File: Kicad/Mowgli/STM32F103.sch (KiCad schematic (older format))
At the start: 1 part

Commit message: added LIS example code
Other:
- note added: "(I2C Accelerometer)"
- note added: "(SPI3 Flash)"
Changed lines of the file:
@@
 encoding utf-8
 Sheet 3 9
-Title ""
-Date ""
-Rev ""
+Title "Project Mowgli"
+Date "2022-05-22"
+Rev "1.0.1"
 Comp ""
-Comment1 ""
-Comment2 ""
+Comment1 "(c) CyberNet / cn@warp.at"
+Comment2 "https://github.com/cloudn1ne/Mowgli"
 Comment3 ""
 Comment4 ""
@@
 Wire Wire Line
 	7200 3800 6450 3800
+Text Notes 7700 3800 0    50   ~ 0
+(I2C Accelerometer)
+Text Notes 7650 3550 0    50   ~ 0
+(SPI3 Flash)
 $EndSCHEMATC

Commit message: updated Kicad with Charge/Battery Circuit
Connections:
- net CHARGE_LOW_SIDE_DRIVER: now reaches U?.39 (PE8)
- net CHARGE_HIGHSIDE_DRIVER: now reaches U?.40 (PE9)
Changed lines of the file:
@@
 $Descr A4 11693 8268
 encoding utf-8
-Sheet 3 9
+Sheet 3 10
 Title "Project Mowgli"
 Date "2022-05-22"
@@
 Text Notes 7650 3550 0    50   ~ 0
 (SPI3 Flash)
+Text HLabel 3700 3900 0    50   Output ~ 0
+CHARGE_LOW_SIDE_DRIVER
+Text HLabel 3700 4000 0    50   Output ~ 0
+CHARGE_HIGHSIDE_DRIVER
+Wire Wire Line
+	4450 3900 3700 3900
+Wire Wire Line
+	4450 4000 3700 4000
 $EndSCHEMATC

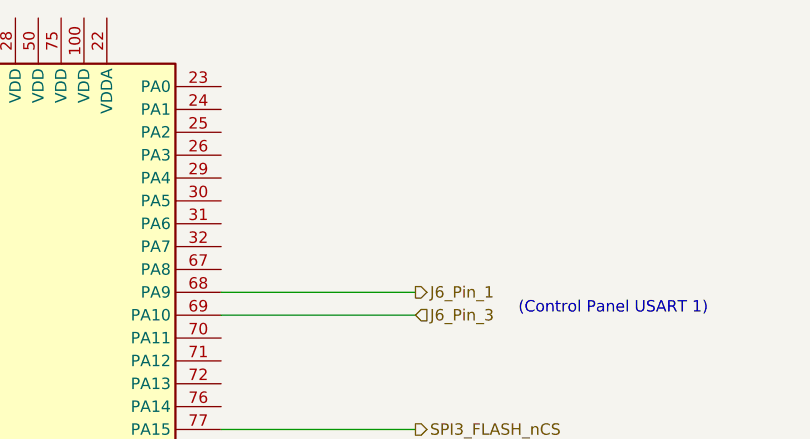
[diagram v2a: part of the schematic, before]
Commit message: added PA3 ADC input pin
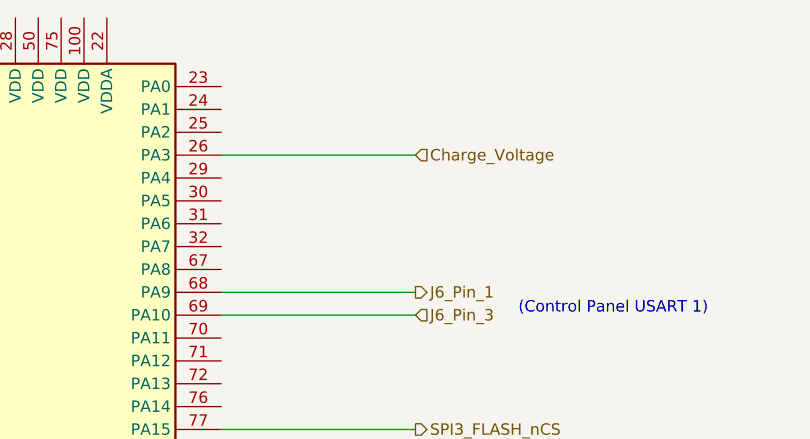
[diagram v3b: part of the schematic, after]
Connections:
- net Charge_Voltage: now reaches U?.26 (PA3)
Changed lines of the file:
@@
 Wire Wire Line
 	4450 4000 3700 4000
+Text HLabel 7300 1700 2    50   Input ~ 0
+Charge_Voltage
+Wire Wire Line
+	7300 1700 6450 1700
 $EndSCHEMATC

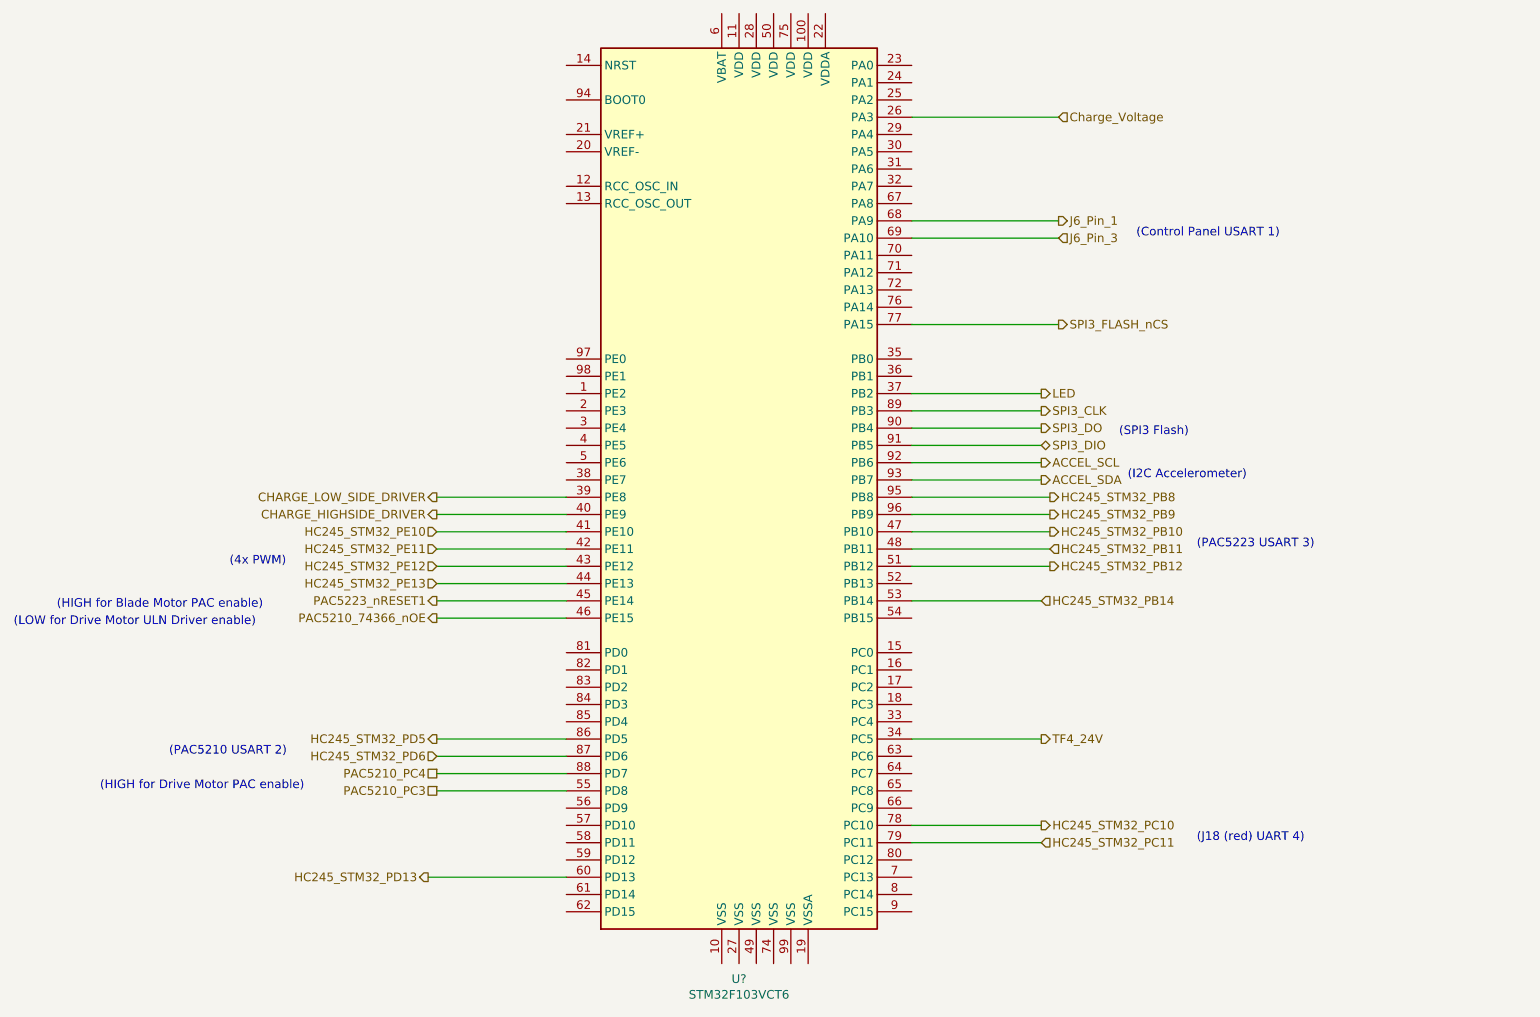
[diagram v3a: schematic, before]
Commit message: added in/out ports that could be found in ghidra
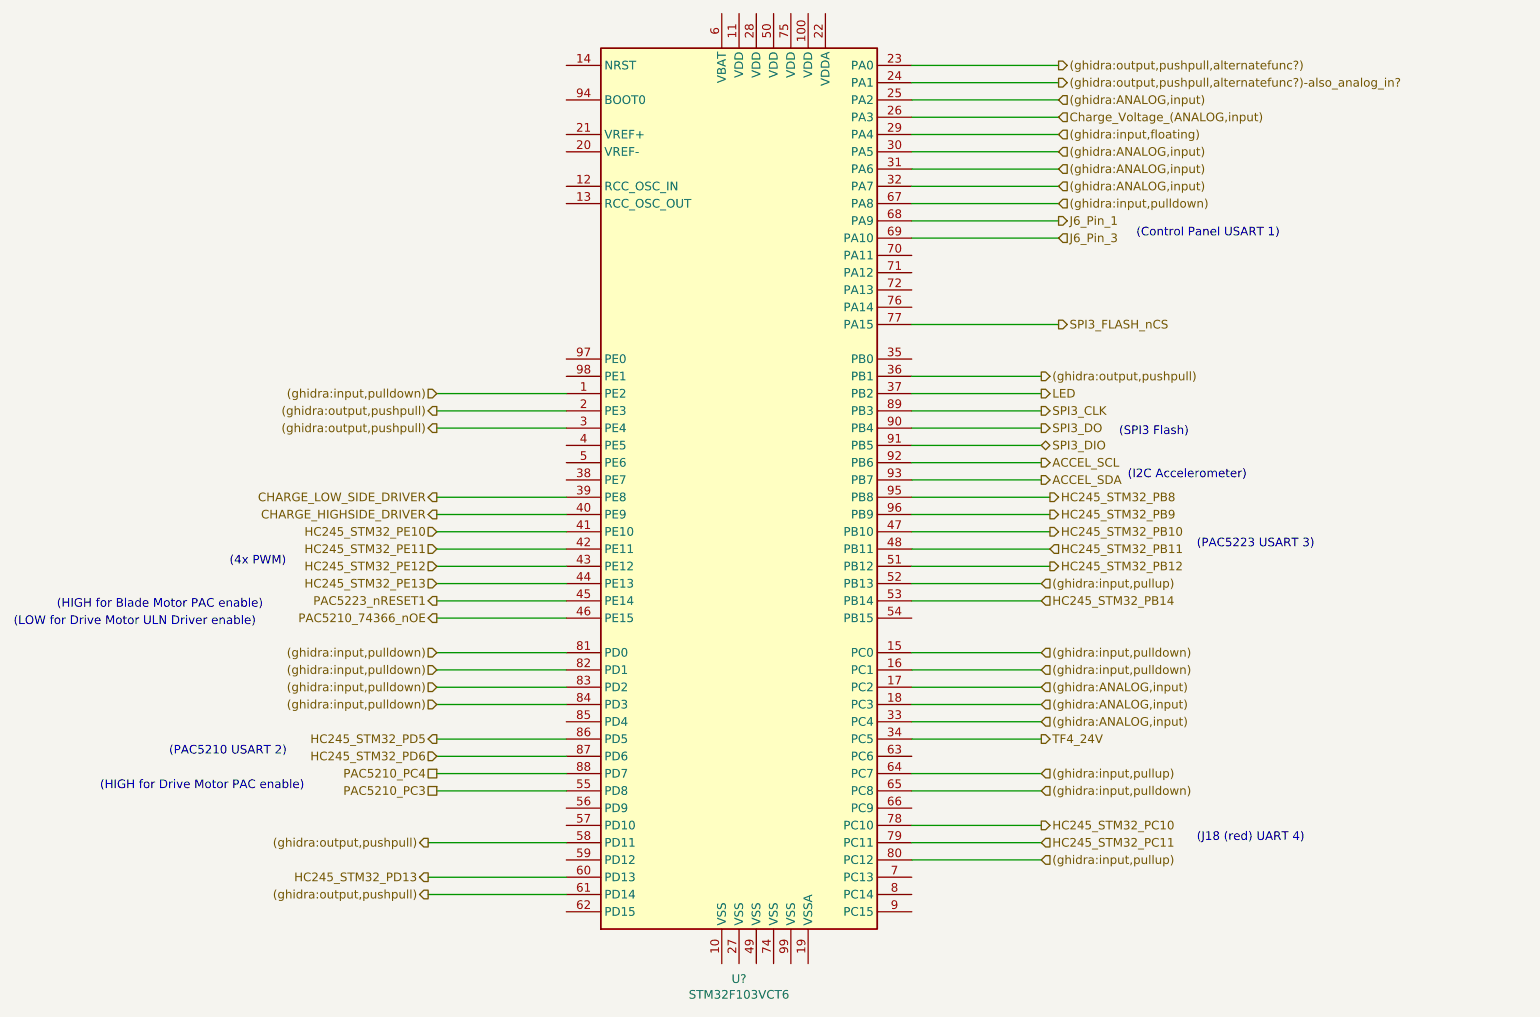
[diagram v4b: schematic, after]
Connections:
- net (ghidra:input,pulldown): now reaches U?.1 (PE2)
- net (ghidra:input,pulldown): now also U?.15 (PC0), U?.16 (PC1), U?.65 (PC8), U?.67 (PA8), U?.81 (PD0), U?.82 (PD1), U?.83 (PD2), U?.84 (PD3)
- net (ghidra:ANALOG,input): now reaches U?.17 (PC2)
- net (ghidra:ANALOG,input): now also U?.18 (PC3), U?.25 (PA2), U?.30 (PA5), U?.31 (PA6), U?.32 (PA7), U?.33 (PC4)
- net (ghidra:output,pushpull): now reaches U?.2 (PE3)
- net (ghidra:output,pushpull): now also U?.3 (PE4), U?.36 (PB1), U?.58 (PD11), U?.61 (PD14)
- net (ghidra:output,pushpull,alternatefunc?): now reaches U?.23 (PA0)
- net (ghidra:output,pushpull,alternatefunc?)-also_analog_in?: now reaches U?.24 (PA1)
- net (ghidra:input,floating): now reaches U?.29 (PA4)
- net (ghidra:input,pullup): now reaches U?.52 (PB13)
- net (ghidra:input,pullup): now also U?.64 (PC7), U?.80 (PC12)
- net Charge_Voltage renamed Charge_Voltage_(ANALOG,input)
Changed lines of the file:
@@
 	4450 4000 3700 4000
 Text HLabel 7300 1700 2    50   Input ~ 0
-Charge_Voltage
+Charge_Voltage_(ANALOG,input)
 Wire Wire Line
 	7300 1700 6450 1700
+Text HLabel 7300 2200 2    50   Input ~ 0
+(ghidra:input,pulldown)
+Wire Wire Line
+	7300 2200 6450 2200
+Text HLabel 3700 5000 0    50   Input ~ 0
+(ghidra:input,pulldown)
+Text HLabel 3700 5100 0    50   Input ~ 0
+(ghidra:input,pulldown)
+Wire Wire Line
+	4450 5100 3700 5100
+Wire Wire Line
+	3700 5000 4450 5000
+Text HLabel 3700 4900 0    50   Input ~ 0
+(ghidra:input,pulldown)
+Text HLabel 3700 4800 0    50   Input ~ 0
+(ghidra:input,pulldown)
+Wire Wire Line
+	4450 4800 3700 4800
+Wire Wire Line
+	4450 4900 3700 4900
+Text HLabel 7300 1400 2    50   Output ~ 0
+(ghidra:output,pushpull,alternatefunc?)
+Text HLabel 7300 1500 2    50   Output ~ 0
+(ghidra:output,pushpull,alternatefunc?)-also_analog_in?
+Wire Wire Line
+	6450 1400 7300 1400
+Text HLabel 7300 1600 2    50   Input ~ 0
+(ghidra:ANALOG,input)
+Wire Wire Line
+	7300 1600 6450 1600
+Wire Wire Line
+	7300 1500 6450 1500
+Text HLabel 7300 1900 2    50   Input ~ 0
+(ghidra:ANALOG,input)
+Text HLabel 7300 2000 2    50   Input ~ 0
+(ghidra:ANALOG,input)
+Text HLabel 7300 2100 2    50   Input ~ 0
+(ghidra:ANALOG,input)
+Wire Wire Line
+	7300 2100 6450 2100
+Wire Wire Line
+	6450 2000 7300 2000
+Wire Wire Line
+	7300 1900 6450 1900
+Text HLabel 7200 5000 2    50   Input ~ 0
+(ghidra:ANALOG,input)
+Text HLabel 7200 5100 2    50   Input ~ 0
+(ghidra:ANALOG,input)
+Text HLabel 7200 5200 2    50   Input ~ 0
+(ghidra:ANALOG,input)
+Wire Wire Line
+	7200 5200 6450 5200
+Wire Wire Line
+	6450 5100 7200 5100
+Wire Wire Line
+	7200 5000 6450 5000
+Text HLabel 7200 4400 2    50   Input ~ 0
+(ghidra:input,pullup)
+Wire Wire Line
+	7200 4400 6450 4400
+Text HLabel 7200 5500 2    50   Input ~ 0
+(ghidra:input,pullup)
+Wire Wire Line
+	7200 5500 6450 5500
+Text HLabel 7200 3200 2    50   Output ~ 0
+(ghidra:output,pushpull)
+Wire Wire Line
+	7200 3200 6450 3200
+Text HLabel 7200 4900 2    50   Input ~ 0
+(ghidra:input,pulldown)
+Wire Wire Line
+	7200 4900 6450 4900
+Text HLabel 7200 4800 2    50   Input ~ 0
+(ghidra:input,pulldown)
+Wire Wire Line
+	7200 4800 6450 4800
+Text HLabel 7200 5600 2    50   Input ~ 0
+(ghidra:input,pulldown)
+Wire Wire Line
+	7200 5600 6450 5600
+Text HLabel 3700 3300 0    50   Input ~ 0
+(ghidra:input,pulldown)
+Wire Wire Line
+	4450 3300 3700 3300
+Text HLabel 7200 6000 2    50   Input ~ 0
+(ghidra:input,pullup)
+Wire Wire Line
+	7200 6000 6450 6000
+Text HLabel 3650 6200 0    50   Output ~ 0
+(ghidra:output,pushpull)
+Wire Wire Line
+	4450 6200 3650 6200
+Text HLabel 3650 5900 0    50   Output ~ 0
+(ghidra:output,pushpull)
+Wire Wire Line
+	4450 5900 3650 5900
+Text HLabel 3700 3400 0    50   Output ~ 0
+(ghidra:output,pushpull)
+Wire Wire Line
+	4450 3400 3700 3400
+Text HLabel 3700 3500 0    50   Output ~ 0
+(ghidra:output,pushpull)
+Wire Wire Line
+	4450 3500 3700 3500
+Text HLabel 7300 1800 2    50   Input ~ 0
+(ghidra:input,floating)
+Wire Wire Line
+	7300 1800 6450 1800
 $EndSCHEMATC

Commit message: PA2,PA3 are used for Charging and Battery Voltage monitoring - added stm32 code and updated KiCad
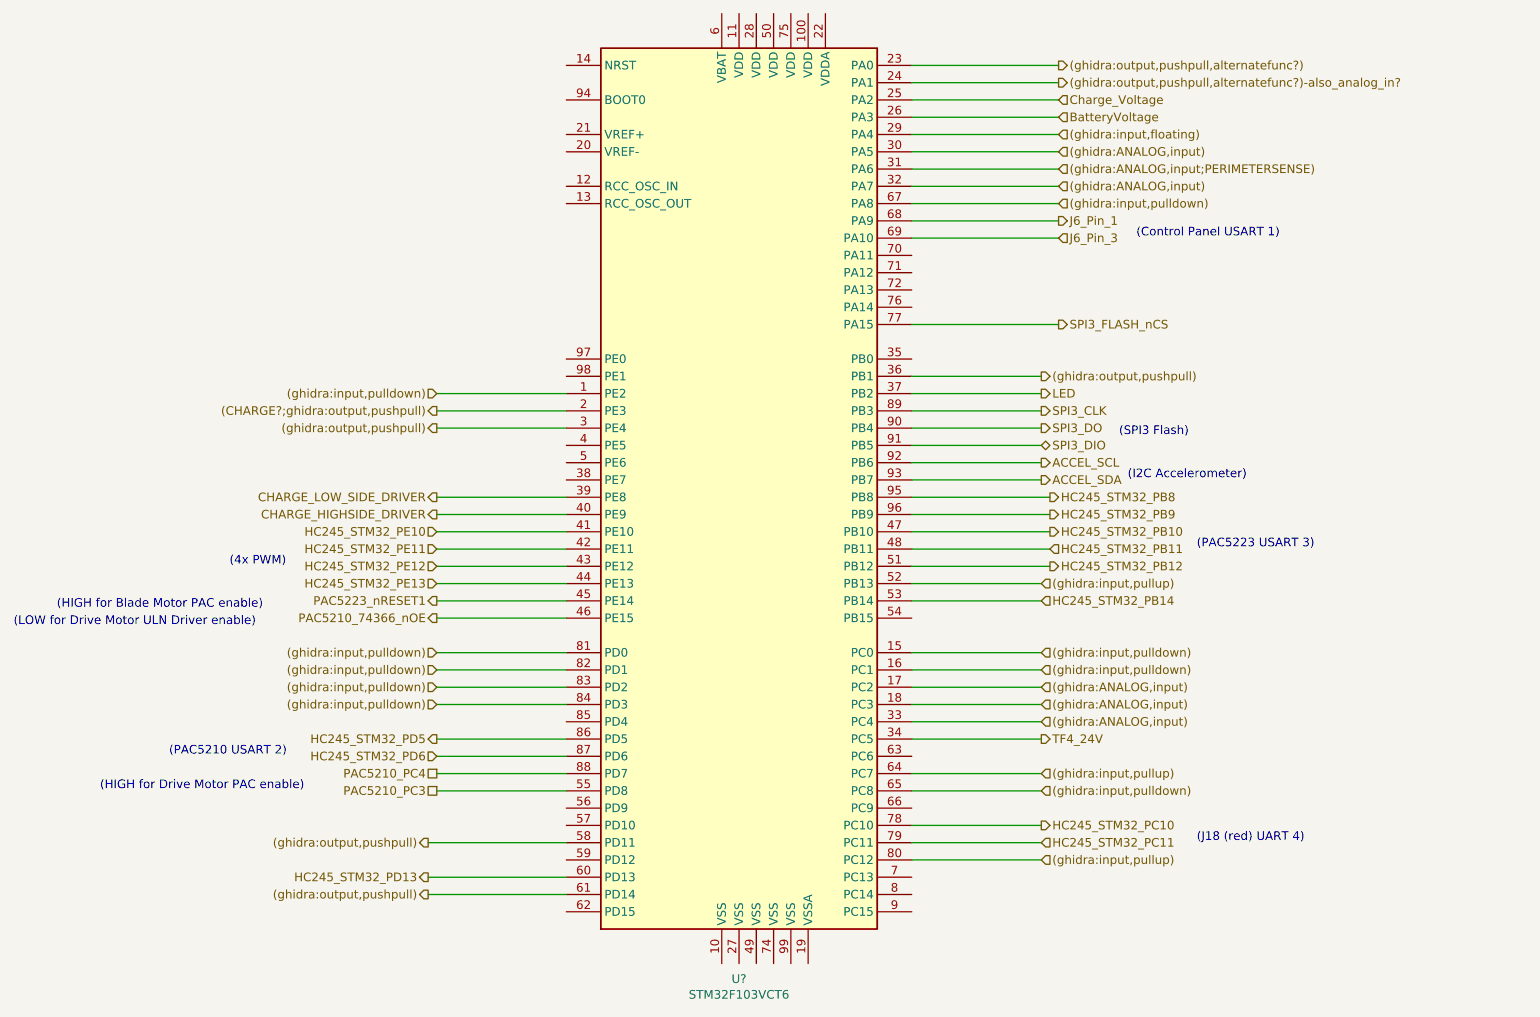
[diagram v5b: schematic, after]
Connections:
- net (ghidra:ANALOG,input): no longer U?.25 (PA2), U?.31 (PA6)
- net (ghidra:output,pushpull): no longer U?.2 (PE3)
- net Charge_Voltage_(ANALOG,input) renamed BatteryVoltage
- new net (CHARGE?;ghidra:output,pushpull): U?.2 (PE3)
- new net (ghidra:ANALOG,input;PERIMETERSENSE): U?.31 (PA6)
- new net Charge_Voltage: U?.25 (PA2)
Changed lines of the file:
@@
 Wire Wire Line
 	4450 4000 3700 4000
-Text HLabel 7300 1700 2    50   Input ~ 0
-Charge_Voltage_(ANALOG,input)
 Wire Wire Line
 	7300 1700 6450 1700
@@
 Wire Wire Line
 	6450 1400 7300 1400
-Text HLabel 7300 1600 2    50   Input ~ 0
-(ghidra:ANALOG,input)
 Wire Wire Line
 	7300 1600 6450 1600
@@
 (ghidra:ANALOG,input)
 Text HLabel 7300 2000 2    50   Input ~ 0
-(ghidra:ANALOG,input)
+(ghidra:ANALOG,input;PERIMETERSENSE)
 Text HLabel 7300 2100 2    50   Input ~ 0
 (ghidra:ANALOG,input)
@@
 	4450 5900 3650 5900
 Text HLabel 3700 3400 0    50   Output ~ 0
-(ghidra:output,pushpull)
+(CHARGE?;ghidra:output,pushpull)
 Wire Wire Line
 	4450 3400 3700 3400
@@
 Wire Wire Line
 	7300 1800 6450 1800
+Text HLabel 7300 1700 2    50   Input ~ 0
+BatteryVoltage
+Text HLabel 7300 1600 2    50   Input ~ 0
+Charge_Voltage
 $EndSCHEMATC

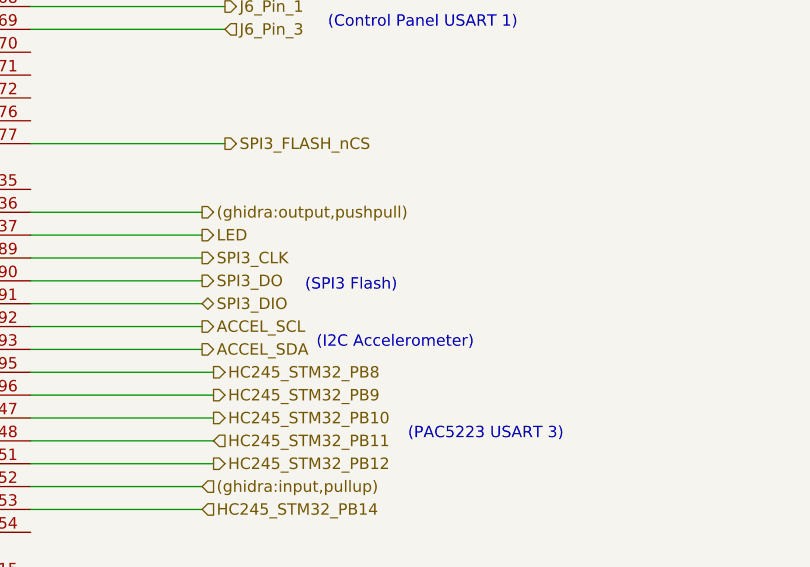
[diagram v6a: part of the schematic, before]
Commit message: added soft i2c and pololu IMU reading support
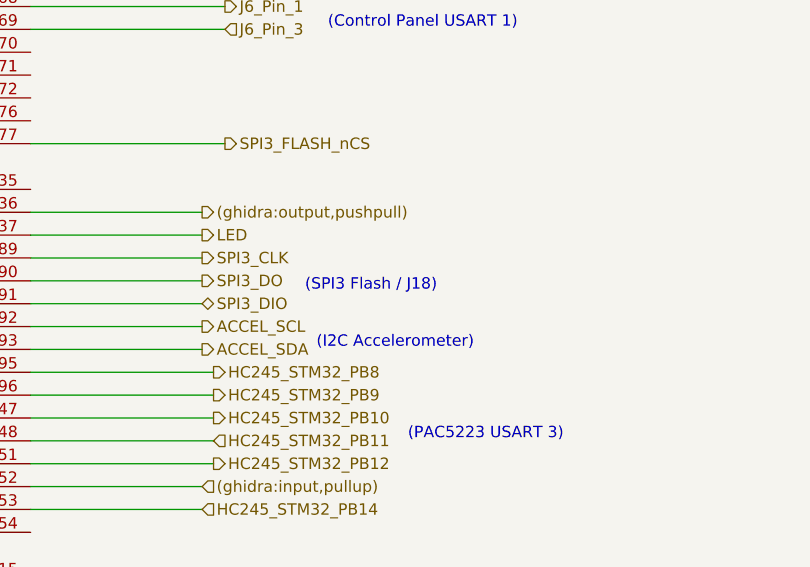
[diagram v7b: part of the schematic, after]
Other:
- note added: "(SPI3 Flash / J18)"
- note removed: "(SPI3 Flash)"
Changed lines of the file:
@@
 (I2C Accelerometer)
 Text Notes 7650 3550 0    50   ~ 0
-(SPI3 Flash)
+(SPI3 Flash / J18)
 Text HLabel 3700 3900 0    50   Output ~ 0
 CHARGE_LOW_SIDE_DRIVER

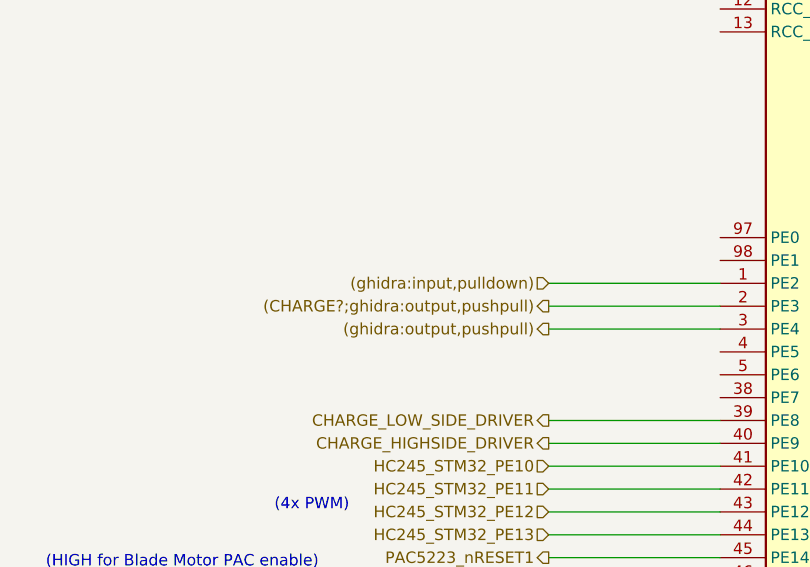
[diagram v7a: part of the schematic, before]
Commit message: added more details to panel J6 connector, and reversed rain sensor (STM32 PE2)
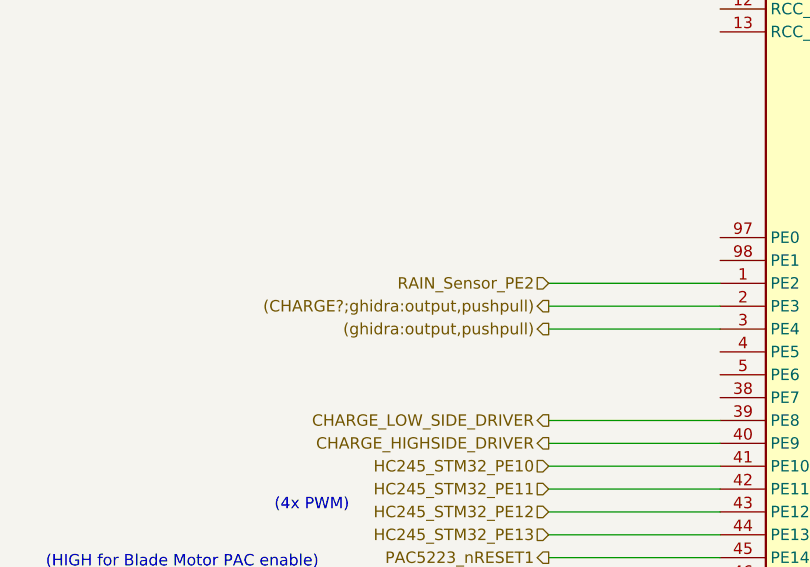
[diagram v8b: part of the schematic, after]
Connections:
- net (ghidra:input,pulldown): no longer U?.1 (PE2)
- new net RAIN_Sensor_PE2: U?.1 (PE2)
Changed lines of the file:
@@
 $Descr A4 11693 8268
 encoding utf-8
-Sheet 3 11
+Sheet 3 12
 Title "Project Mowgli"
 Date "2022-05-22"
@@
 	7200 5600 6450 5600
 Text HLabel 3700 3300 0    50   Input ~ 0
-(ghidra:input,pulldown)
+RAIN_Sensor_PE2
 Wire Wire Line
 	4450 3300 3700 3300
